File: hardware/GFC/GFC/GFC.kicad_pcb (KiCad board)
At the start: 2 copper layers, 53 parts, among them J1 BAT, J2 Pi Zero/Zero W, J3 USB Sound Card Connection, Q1 Q_NPN_BCE, Q2 DMN67D8LW-13, Q3 Q_NPN_BCE, SW1 H/L_DIP_SW, T1 DS18B20 - Connector, T2 DS18B20 - Connector, T3 DS18B20 - Connector, U1 MAX17048G+T10, U2 LTV-356T, U3 BMP390L, U4 SAM-M8Q

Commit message: Sync PCB
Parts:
- added VR2: LD29150PTR, footprints:LD29150PTR, F.Cu at (34.4, 33.7)
- AE1: value Antenna_Shield -> Antenna
- J2: footprint Connector_PinSocket_2.54mm:PinSocket_2x20_P2.54mm_Vertical -> Connector_PinSocket_2.54mm:PinSocket_2x20_P2.54mm_Vertical_SMD
- moved RV1 115.2 mm to (191.1, 111.6), turned to 180 degrees
- moved C2 110.7 mm to (39.5, 59.7), turned to 90 degrees
- moved R11 100.9 mm to (37.0, 27.3), turned to 180 degrees
- moved R12 99.7 mm to (42.0, 28.0), turned to 90 degrees
- moved C14 97.1 mm to (188.4, 116.1), turned to 180 degrees
- moved R2 96.4 mm to (158.1, 73.0), turned to 90 degrees
- moved T2 93.9 mm to (100.7, 64.8), turned to 180 degrees
- moved Q1 93.4 mm to (161.3, 73.0), turned to 180 degrees
- moved C19 90.3 mm to (45.2, 31.1)
- moved C5 90.1 mm to (44.8, 38.8)
- moved C18 88.1 mm to (44.8, 36.9)
- moved Q3 86.7 mm to (172.2, 99.7), turned to 180 degrees
- moved C4 86.7 mm to (30.8, 55.3), turned to 180 degrees
- moved C13 82.7 mm to (179.5, 112.3)
- moved C3 81.6 mm to (33.8, 59.1), turned to -90 degrees
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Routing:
- net +3V3: track 0.00 -> 221.2 mm, vias 0 -> 15
- net /BMP390 (I2C)/SDA: track 0.00 -> 149.3 mm, vias 0 -> 8
- net /BMP390 (I2C)/SCL: track 0.00 -> 99.4 mm, vias 0 -> 8
- net /Power/4.3V: track 0.00 -> 90.2 mm
- net GND: track 0.00 -> 85.8 mm, vias 0 -> 6
- net /DRA818/DRA TXD: track 0.00 -> 51.3 mm
- net /Power/5V: track 0.00 -> 40.3 mm
- net Net-(C13-Pad1): track 0.00 -> 35.7 mm, vias 0 -> 2
- net /DRA818/DRA RXD: track 0.00 -> 28.1 mm
- net Net-(J2-Pad7): track 0.00 -> 21.7 mm
- net VCC: track 0.00 -> 20.8 mm
- net Net-(C2-Pad1): track 0.00 -> 20.7 mm
- net Net-(C6-Pad1): track 0.00 -> 17.0 mm
- net /DRA818/V4.3: track 0.00 -> 9.76 mm
- net Net-(C9-Pad1): track 0.00 -> 8.57 mm
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- added copper zone on F.Cu, net GND
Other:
- rule pad_to_mask_clearance: 0 -> 0.0508

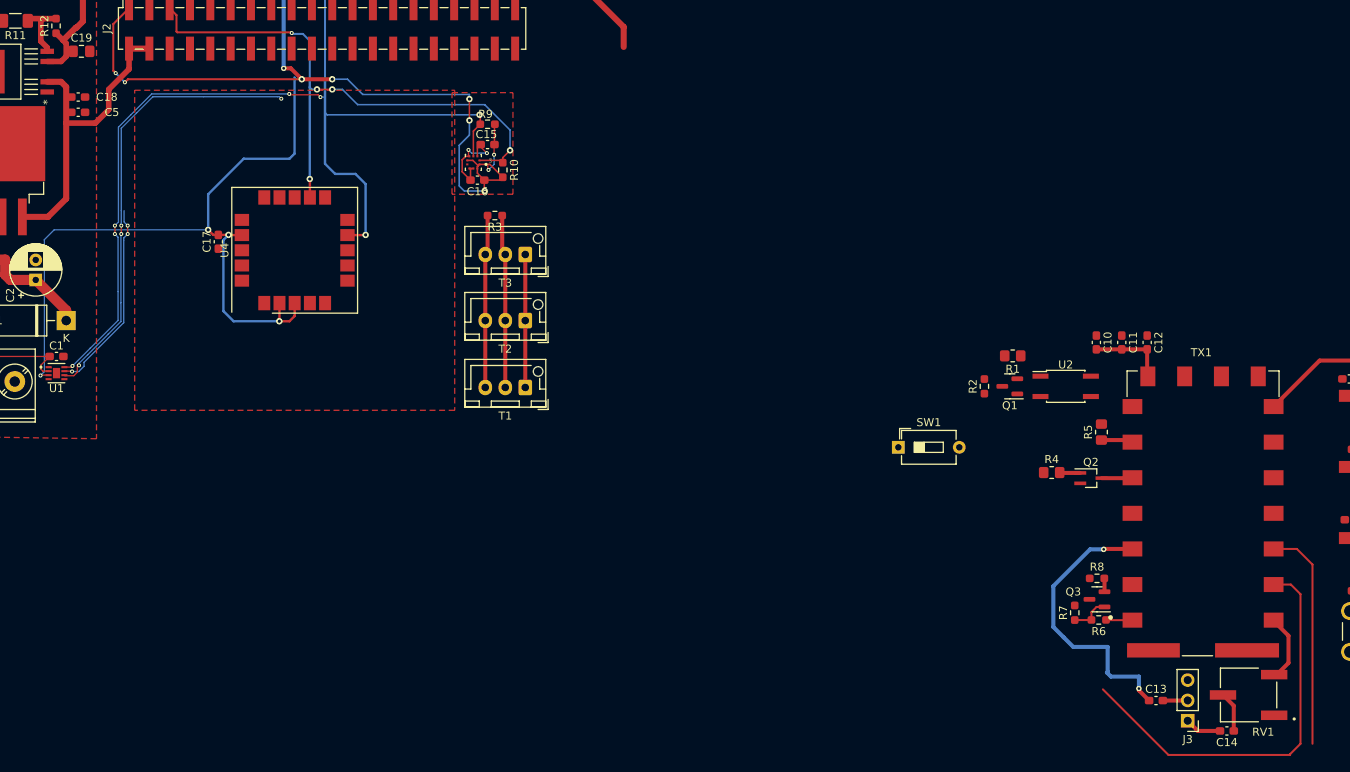
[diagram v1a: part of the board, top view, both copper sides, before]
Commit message: Schematic Update - ADC/DAC & GPIO Config EEPROM
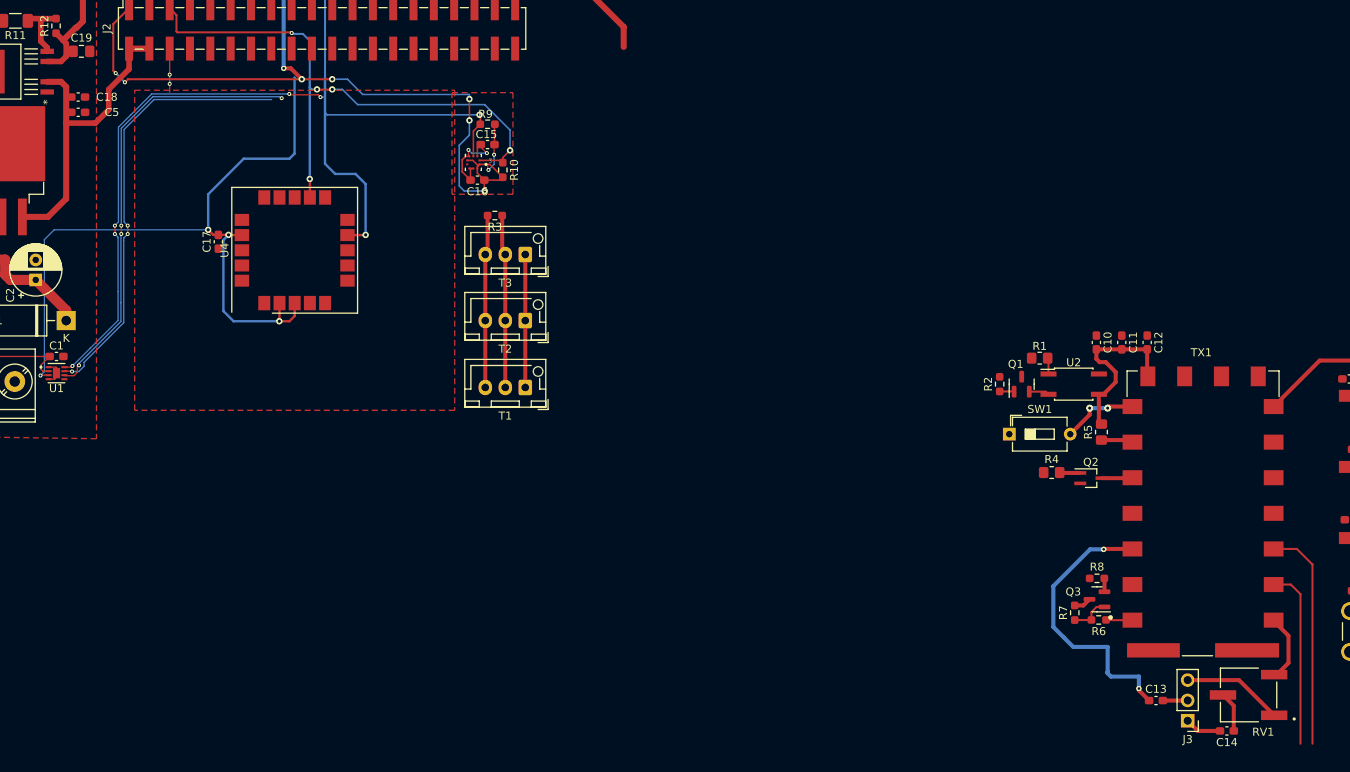
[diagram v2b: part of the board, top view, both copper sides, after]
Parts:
- moved SW1 14.0 mm to (161.2, 79.0)
- moved R1 3.38 mm to (165.0, 69.5)
- moved R2 1.93 mm to (160.0, 72.8)
- moved Q1 1.51 mm to (162.8, 72.8), turned to 90 degrees
- moved U2 1.04 mm to (169.2, 72.8)
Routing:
- net /BMP390 (I2C)/SCL: track 99.4 -> 129.5 mm
- net /DRA818/DRA TXD: track 51.3 -> 22.6 mm
- net GND: track 85.8 -> 108.4 mm, vias 6 -> 8
- net /DRA818/V4.3: track 9.76 -> 21.9 mm
- net Net-(SW1-Pad2): track 0.00 -> 9.68 mm, vias 0 -> 2
- net Net-(Q1-Pad2): track 0.00 -> 2.54 mm
- net Net-(R1-Pad1): track 0.00 -> 2.02 mm
- net Net-(Q1-Pad1): track 0.00 -> 1.81 mm

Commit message: sync
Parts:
- removed J2: Pi Zero/Zero W, Connector_PinSocket_2.54mm:PinSocket_2x20_P2.54mm_Vertical_SMD
- removed J3: USB Sound Card Connection, Connector_PinHeader_2.54mm:PinHeader_1x03_P2.54mm_Vertical
- removed R2: ?, Resistor_SMD:R_0603_1608Metric_Pad0.98x0.95mm_HandSolder
- removed T1, T2, T3: DS18B20 - Connector, Connector_JST:JST_XH_B3B-XH-AM_1x03_P2.50mm_Vertical
- removed U1: MAX17048G+T10, MAX17048G_T10:SON50P200X200X80-9N
- removed U3: BMP390L, BMP390:XDCR_BMP390L
- added C21: 1uF, Capacitor_SMD:C_0603_1608Metric_Pad1.08x0.95mm_HandSolder, F.Cu at (165.4, 56.3)
- added C26: 1uF, Capacitor_SMD:C_0603_1608Metric_Pad1.08x0.95mm_HandSolder, F.Cu at (175.9, 46.8)
- added C29: 1uF, Capacitor_SMD:C_0603_1608Metric_Pad1.08x0.95mm_HandSolder, F.Cu at (169.7, 56.3)
- added C30: 1uF, Capacitor_SMD:C_0603_1608Metric_Pad1.08x0.95mm_HandSolder, F.Cu at (165.4, 58.9)
- added C33: 1uF, Capacitor_SMD:C_0603_1608Metric_Pad1.08x0.95mm_HandSolder, F.Cu at (175.9, 44.3)
- added CPU1: Pi Zero/Zero W, Connector_PinSocket_2.54mm:PinSocket_2x20_P2.54mm_Vertical, F.Cu at (55.4, 51.8)
- added R13: ?, Resistor_SMD:R_0603_1608Metric_Pad0.98x0.95mm_HandSolder, F.Cu at (45.7, 218.7)
- added TMP1: DS18B20 - Connector, Connector_JST:JST_XH_B3B-XH-AM_1x03_P2.50mm_Vertical, F.Cu at (190.8, 62.3)
- added TMP2: DS18B20 - Connector, Connector_JST:JST_XH_B3B-XH-AM_1x03_P2.50mm_Vertical, F.Cu at (190.8, 55.4)
- added TMP3: DS18B20 - Connector, Connector_JST:JST_XH_B3B-XH-AM_1x03_P2.50mm_Vertical, F.Cu at (190.8, 48.5)
- added TP1: Test Point, TestPoint:TestPoint_Pad_D1.0mm, F.Cu at (51.8, 231.4)
- added TP10: Test Point, TestPoint:TestPoint_Pad_D1.0mm, F.Cu at (83.3, 49.0)
- added TP11: Test Point, TestPoint:TestPoint_Pad_D1.0mm, F.Cu at (88.4, 49.0)
- added TP12: Test Point, TestPoint:TestPoint_Pad_D1.0mm, F.Cu at (90.9, 49.0)
- added TP13: Test Point, TestPoint:TestPoint_Pad_D1.0mm, F.Cu at (63.0, 57.1)
- added TP14: Test Point, TestPoint:TestPoint_Pad_D1.0mm, F.Cu at (65.5, 57.1)
- added TP15: Test Point, TestPoint:TestPoint_Pad_D1.0mm, F.Cu at (68.1, 57.1)
- added TP16: Test Point, TestPoint:TestPoint_Pad_D1.0mm, F.Cu at (83.3, 57.1)
- added TP17: Test Point, TestPoint:TestPoint_Pad_D1.0mm, F.Cu at (85.9, 57.1)
- added TP18: Test Point, TestPoint:TestPoint_Pad_D1.0mm, F.Cu at (88.4, 57.1)
- added TP19: Test Point, TestPoint:TestPoint_Pad_D1.0mm, F.Cu at (56.1, 234.4)
- added TP2: Test Point, TestPoint:TestPoint_Pad_D1.0mm, F.Cu at (55.4, 49.0)
- added TP20: Test Point, TestPoint:TestPoint_Pad_D1.0mm, F.Cu at (56.6, 225.8)
- added TP21: Test Point, TestPoint:TestPoint_Pad_D1.0mm, F.Cu at (52.6, 235.5)
- added TP22: Test Point, TestPoint:TestPoint_Pad_D1.0mm, F.Cu at (64.0, 212.3)
- added TP23: Test Point, TestPoint:TestPoint_Pad_D1.0mm, F.Cu at (55.1, 247.4)
- added TP24: Test Point, TestPoint:TestPoint_Pad_D1.0mm, F.Cu at (67.6, 255.5)
- added TP25: Test Point, TestPoint:TestPoint_Pad_D1.0mm, F.Cu at (47.5, 255.5)
- added TP26: Test Point, TestPoint:TestPoint_Pad_D1.0mm, F.Cu at (55.9, 210.6)
- added TP27: Test Point, TestPoint:TestPoint_Pad_D1.0mm, F.Cu at (50.8, 223.8)
- added TP28: Test Point, TestPoint:TestPoint_Pad_D1.0mm, F.Cu at (47.5, 211.8)
- added TP29: Test Point, TestPoint:TestPoint_Pad_D1.0mm, F.Cu at (26.9, 31.2)
- added TP3: Test Point, TestPoint:TestPoint_Pad_D1.0mm, F.Cu at (57.9, 49.0)
- added TP30: Test Point, TestPoint:TestPoint_Pad_D1.0mm, F.Cu at (47.0, 52.8)
- added TP31: Test Point, TestPoint:TestPoint_Pad_D1.0mm, F.Cu at (19.1, 35.6)
- added TP32: Test Point, TestPoint:TestPoint_Pad_D1.0mm, F.Cu at (51.4, 38.4)
- added TP33: Test Point, TestPoint:TestPoint_Pad_D1.0mm, F.Cu at (44.2, 57.7)
- added TP34: Test Point, TestPoint:TestPoint_Pad_D1.0mm, F.Cu at (19.3, 50.0)
- added TP35: Test Point, TestPoint:TestPoint_Pad_D1.0mm, F.Cu at (57.5, 38.4)
- added TP36: Test Point, TestPoint:TestPoint_Pad_D1.0mm, F.Cu at (20.8, 63.8)
- added TP37: Test Point, TestPoint:TestPoint_Pad_D1.0mm, F.Cu at (216.1, 50.1)
- added TP38: Test Point, TestPoint:TestPoint_Pad_D1.0mm, F.Cu at (219.1, 47.6)
- added TP39: Test Point, TestPoint:TestPoint_Pad_D1.0mm, F.Cu at (216.1, 47.1)
- added TP4: Test Point, TestPoint:TestPoint_Pad_D1.0mm, F.Cu at (60.5, 49.0)
- added TP40: Test Point, TestPoint:TestPoint_Pad_D1.0mm, F.Cu at (220.4, 44.6)
- added TP41: Test Point, TestPoint:TestPoint_Pad_D1.0mm, F.Cu at (211.7, 52.1)
- added TP42: Test Point, TestPoint:TestPoint_Pad_D1.0mm, F.Cu at (158.3, 119.0)
- added TP43: Test Point, TestPoint:TestPoint_Pad_D1.0mm, F.Cu at (175.3, 99.4)
- added TP44: Test Point, TestPoint:TestPoint_Pad_D1.0mm, F.Cu at (193.3, 44.7)
- added TP45: Test Point, TestPoint:TestPoint_Pad_D1.0mm, F.Cu at (195.8, 44.7)
- added TP5: Test Point, TestPoint:TestPoint_Pad_D1.0mm, F.Cu at (63.0, 49.0)
- added TP6: Test Point, TestPoint:TestPoint_Pad_D1.0mm, F.Cu at (70.6, 49.0)
- added TP7: Test Point, TestPoint:TestPoint_Pad_D1.0mm, F.Cu at (73.2, 49.0)
- added TP8: Test Point, TestPoint:TestPoint_Pad_D1.0mm, F.Cu at (78.2, 49.0)
- added TP9: Test Point, TestPoint:TestPoint_Pad_D1.0mm, F.Cu at (80.8, 49.0)
- added U5: PCM2902C, Package_SO:SSOP-28_5.3x10.2mm_P0.65mm, F.Cu at (168.5, 49.1)
- added U6: CAT24C32WI-GT3, footprints:SOIC127P600X175-8N, F.Cu at (140.2, 95.5)
- R1: value 100 -> 4.7k; footprint Resistor_SMD:R_0805_2012Metric_Pad1.20x1.40mm_HandSolder -> Resistor_SMD:R_0603_1608Metric_Pad0.98x0.95mm_HandSolder
- R3: value 4.7k -> 100; footprint Resistor_SMD:R_0603_1608Metric_Pad0.98x0.95mm_HandSolder -> Resistor_SMD:R_0805_2012Metric_Pad1.20x1.40mm_HandSolder
- moved RV1 194.3 mm to (60.6, 255.5)
- moved L1 188.0 mm to (88.4, 222.8)
- moved Q2 187.6 mm to (55.4, 231.9)
- moved C7 187.5 mm to (87.1, 226.8)
- moved L2 187.4 mm to (88.4, 230.9)
- moved C6 187.3 mm to (87.1, 218.7), turned to 0 degrees
- moved L3 186.8 mm to (88.4, 239.0)
- moved C8 186.4 mm to (87.1, 234.9)
- moved R5 186.4 mm to (55.6, 223.8), turned to 180 degrees
- moved C9 186.3 mm to (87.4, 243.1)
- moved AE1 185.8 mm to (89.2, 247.9)
- moved C12 185.5 mm to (62.2, 212.1)
- moved TX1 184.9 mm to (69.1, 232.7)
- moved C11 184.4 mm to (60.7, 212.1)
- moved R6 183.9 mm to (56.9, 245.4), turned to 90 degrees
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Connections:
- net /DRA818/SQ GPIO renamed GPIO.DRA_SQ
- net /DRA818/V4.3 renamed /DRA818/4V3 Controlled
- net /Power/4.3V renamed +4V3
- net /Power/5V renamed +5V
- net Net-(C2-Pad1) renamed /Power/VCC_P
- net Net-(R6-Pad1) renamed /DRA818/DRA SQ
- C13 pad 2: Net-(C13-Pad2) -> /DAC/AUDIO.SC_IN_R
- C14 pad 1: Net-(C14-Pad1) -> Net-(RV1-Pad3)
- C14 pad 2: Net-(C14-Pad2) -> Net-(TX1-Pad18)
- R1 pad 1: Net-(R1-Pad1) -> 1-Wire
- R10 pad 1: /BMP390 (I2C)/SCL -> /BMP390 (I2C)/I2C0.SCL
- R3 pad 1: Net-(J2-Pad7) -> Net-(R3-Pad1)
- R4 pad 1: /DRA818/PTT GPIO -> GPIO.DRA_PTT
- R9 pad 2: /BMP390 (I2C)/SDA -> /BMP390 (I2C)/I2C0.SDA
- RV1 pad 2: Net-(C14-Pad1) -> /DAC/AUDIO.SC_OUT_R
- TX1 pad 16: /DRA818/DRA RXD -> UART0.PI_TXD
- TX1 pad 17: /DRA818/DRA TXD -> UART0.PI_RXD
- TX1 pad 18: Net-(RV1-Pad3) -> Net-(TX1-Pad18)
- U2 pad 1: Net-(R1-Pad1) -> Net-(R3-Pad1)
- U4 pad 12: /BMP390 (I2C)/SCL -> I2C0.SCL
- U4 pad 9: /BMP390 (I2C)/SDA -> I2C0.SDA
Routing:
- net +3V3: track 221.2 -> 17.6 mm, vias 15 -> 0
- net /BMP390 (I2C)/SDA: track 149.3 -> 0.00 mm, vias 8 -> 0
- net /BMP390 (I2C)/SCL: track 129.5 -> 0.00 mm, vias 8 -> 0
- net GND: track 108.4 -> 16.1 mm, vias 8 -> 0
- net +4V3: track 90.2 -> 31.7 mm
- net Net-(C13-Pad1): track 35.7 -> 0.00 mm, vias 2 -> 0
- net /DRA818/DRA RXD: track 28.1 -> 0.00 mm
- net /DRA818/DRA TXD: track 22.6 -> 0.00 mm
- net Net-(J2-Pad7): track 21.7 -> 0.00 mm
- net 1-Wire: track 0.00 -> 17.6 mm
- net +5V: track 40.3 -> 27.7 mm
- net Net-(SW1-Pad2): track 9.68 -> 0.00 mm, vias 2 -> 0
- net Net-(RV1-Pad3): track 8.51 -> 0.00 mm
- net Net-(C6-Pad1): track 17.0 -> 9.66 mm
- net Net-(C14-Pad1): track 5.06 -> 0.00 mm
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- removed copper zone on F.Cu, net GND
